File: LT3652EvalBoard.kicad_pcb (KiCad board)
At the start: 2 copper layers, 55.2 x 50.3 mm, 42 parts, among them U1 LT3652

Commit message: Fixed project info
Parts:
- Dbat1, Dflybk1, Dvin1: footprint diodes:DIODES_INC_ZLLS500 -> ms_diodes:DIODES_INC_ZLLS500
- Lsw1: footprint inductors:PANASONIC_ELC09D100F -> ms_inductors:PANASONIC_ELC09D100F
- Pload2: footprint connectors:WURTH_ELEKTRONIK_629104151021 -> ms_connectors:WURTH_ELEKTRONIK_629104151021
- RV1, RV2: footprint bourns_trim_pots:Bourns_3362P_Trimmer -> ms_bourns_trim_pots:Bourns_3362P_Trimmer
- Wbat1, Wgnd1, Wshdn1, Wsw1, Wvfb1, Wvreg1: footprint pcb_test_points:HARWIN_S1751-46 -> ms_pcb_test_points:HARWIN_S1751-46
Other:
- board text added: "LT3652 Eval Board Rev 0.3 15-03-2016"
- board text added: "https://github.com/malcolmspiteri/LT3652EvalBoard"
- board text removed: "LT3652 Eval Board Rev 0.3"
- board text removed: "Url: https://github.com/malcolmspiteri/LT3652EvalBoard Date: 13-03-2016"

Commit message: Rev 0.3 Final - onto Rev 0.4 now to make the board smaller hence cheaper to manufacture
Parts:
- U1: footprint ms_lt3652:LT3652MSE_HandSoldering -> ms_lt3652:LT3652MSE
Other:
- rule pad_to_mask_clearance: 0.2 -> 0.055
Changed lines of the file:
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@@
     (pad_size 1.524 1.524)
     (pad_drill 0.762)
-    (pad_to_mask_clearance 0.2)
+    (pad_to_mask_clearance 0.055)
     (aux_axis_origin 147.866 107.95)
     (grid_origin 147.066 107.95)
@@
     )
   )
-  (module ms_lt3652:LT3652MSE_HandSoldering (layer F.Cu)
-    (at 138.666 98.75)
-    (fp_text reference U1 (at 0.02 3.49) (layer F.SilkS)
-      (effects (font (size 0.5 0.5) (thickness 0.075)))
-    )
-    (fp_text value LT3652 (at 0 2.64) (layer F.Fab)
-      (effects (font (size 0.5 0.5) (thickness 0.075)))
-    )
-    (pad 6 smd rect (at -2.258 1.6075 90) (size 0.42 1.3) (layers F.Cu F.Paste F.Mask)
-      (net 6 "Net-(JP1-Pad2)") (solder_mask_margin 0.05))
-    (pad 5 smd rect (at -2.258 0.9575 90) (size 0.42 1.3) (layers F.Cu F.Paste F.Mask)
-      (net 10 "Net-(R2-Pad1)") (solder_mask_margin 0.05))
-    (pad 4 smd rect (at -2.258 0.3075 90) (size 0.42 1.3) (layers F.Cu F.Paste F.Mask)
-      (net 9 "Net-(R1-Pad1)") (solder_mask_margin 0.05))
-    (pad 3 smd rect (at -2.258 -0.3425 90) (size 0.42 1.3) (layers F.Cu F.Paste F.Mask)
-      (net 5 /SHDN) (solder_mask_margin 0.05))
-    (pad 2 smd rect (at -2.258 -0.9925 90) (size 0.42 1.3) (layers F.Cu F.Paste F.Mask)
-      (net 4 /VIN_REG) (solder_mask_margin 0.05))
-    (pad 1 smd rect (at -2.258 -1.6425 90) (size 0.42 1.3) (layers F.Cu F.Paste F.Mask)
-      (net 3 /VIN) (solder_mask_margin 0.05))
-    (pad 12 smd rect (at 2.253 -1.6425 90) (size 0.42 1.3) (layers F.Cu F.Paste F.Mask)
-      (net 17 /SW) (solder_mask_margin 0.05))
-    (pad 11 smd rect (at 2.253 -0.9925 90) (size 0.42 1.3) (layers F.Cu F.Paste F.Mask)
-      (net 16 /BOOST) (solder_mask_margin 0.05))
-    (pad 10 smd rect (at 2.253 -0.3425 90) (size 0.42 1.3) (layers F.Cu F.Paste F.Mask)
-      (net 19 /SENSE) (solder_mask_margin 0.05))
-    (pad 9 smd rect (at 2.253 0.3075 90) (size 0.42 1.3) (layers F.Cu F.Paste F.Mask)
-      (net 15 /BAT) (solder_mask_margin 0.05))
-    (pad 8 smd rect (at 2.253 0.9575 90) (size 0.42 1.3) (layers F.Cu F.Paste F.Mask)
-      (solder_mask_margin 0.05))
-    (pad 7 smd rect (at 2.253 1.6075 90) (size 0.42 1.3) (layers F.Cu F.Paste F.Mask)
-      (net 18 /VFB) (solder_mask_margin 0.05))
-    (pad 13 smd rect (at -0.0075 -0.0175 90) (size 2.845 1.7) (layers F.Cu F.Paste F.Mask)
-      (net 2 GND))
-  )
   (module ms_diodes:DIODES_INC_ZLLS500 (layer F.Cu)
     (at 149.066 104.25)
@@
   (module ms_connectors:WURTH_ELEKTRONIK_629104151021 (layer F.Cu)
     (at 162.466 87.75 90)
-    (fp_text reference Pload2 (at 0 9.6 90) (layer F.SilkS)
+    (fp_text reference Pload2 (at 8.6 -2 180) (layer F.SilkS)
       (effects (font (size 1 1) (thickness 0.15)))
     )
@@
       (net 4 /VIN_REG))
   )
+  (module ms_lt3652:LT3652MSE (layer F.Cu)
+    (at 138.666 98.75)
+    (fp_text reference U1 (at 0.02 3.49) (layer F.SilkS)
+      (effects (font (size 0.5 0.5) (thickness 0.075)))
+    )
+    (fp_text value LT3652 (at 0 2.64) (layer F.Fab)
+      (effects (font (size 0.5 0.5) (thickness 0.075)))
+    )
+    (pad 6 smd rect (at -2.1025 1.6075 90) (size 0.42 0.989) (layers F.Cu F.Paste F.Mask)
+      (net 6 "Net-(JP1-Pad2)"))
+    (pad 5 smd rect (at -2.1025 0.9575 90) (size 0.42 0.989) (layers F.Cu F.Paste F.Mask)
+      (net 10 "Net-(R2-Pad1)"))
+    (pad 4 smd rect (at -2.1025 0.3075 90) (size 0.42 0.989) (layers F.Cu F.Paste F.Mask)
+      (net 9 "Net-(R1-Pad1)"))
+    (pad 3 smd rect (at -2.1025 -0.3425 90) (size 0.42 0.989) (layers F.Cu F.Paste F.Mask)
+      (net 5 /SHDN))
+    (pad 2 smd rect (at -2.1025 -0.9925 90) (size 0.42 0.989) (layers F.Cu F.Paste F.Mask)
+      (net 4 /VIN_REG))
+    (pad 1 smd rect (at -2.1025 -1.6425 90) (size 0.42 0.989) (layers F.Cu F.Paste F.Mask)
+      (net 3 /VIN))
+    (pad 12 smd rect (at 2.0975 -1.6425 90) (size 0.42 0.989) (layers F.Cu F.Paste F.Mask)
+      (net 17 /SW))
+    (pad 11 smd rect (at 2.0975 -0.9925 90) (size 0.42 0.989) (layers F.Cu F.Paste F.Mask)
+      (net 16 /BOOST))
+    (pad 10 smd rect (at 2.0975 -0.3425 90) (size 0.42 0.989) (layers F.Cu F.Paste F.Mask)
+      (net 19 /SENSE))
+    (pad 9 smd rect (at 2.0975 0.3075 90) (size 0.42 0.989) (layers F.Cu F.Paste F.Mask)
+      (net 15 /BAT))
+    (pad 8 smd rect (at 2.0975 0.9575 90) (size 0.42 0.989) (layers F.Cu F.Paste F.Mask))
+    (pad 7 smd rect (at 2.0975 1.6075 90) (size 0.42 0.989) (layers F.Cu F.Paste F.Mask)
+      (net 18 /VFB))
+    (pad 13 smd rect (at -0.0075 -0.0175 90) (size 2.845 1.7) (layers F.Cu F.Paste F.Mask)
+      (net 2 GND))
+  )
   (gr_line (start 162.666 120.55) (end 161.366 120.55) (angle 90) (layer F.SilkS) (width 0.2))

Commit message: Upload of Rev 0.5
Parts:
- removed the ? at (143.9, 95.8)
- removed Pload2: USB_A, ms_connectors:WURTH_ELEKTRONIK_629104151021
- added REF**: MHH-20_ABS_Plastic_Box, ms_enclosures:MHH-20_ABS_Plastic_Box_Holes_Only, F.Cu at (135.4, 89.7)
- added Wvin1: TEST_1P, ms_pcb_test_points:HARWIN_S1751-46, F.Cu at (119.6, 68.4)
- Pbat1, Pload1: footprint w_conn_jst-ph:b2b-ph-kl -> w_conn_jst-ph:s2b-ph-kl
- U1: footprint ms_lt3652:LT3652MSE -> ms_lt3652:LT3652MSE_HandSoldering
- moved Pload1 28.8 mm to (153.3, 76.2)
- moved Cbat1 27.3 mm to (147.3, 75.7), turned to 180 degrees
- moved Wbat1 23.2 mm to (152.3, 85.7), turned to 90 degrees
- moved JPload1 18.1 mm to (152.6, 91.7), turned to 0 degrees
- moved Pbat1 16.0 mm to (153.3, 102.7)
- moved ? 9.92 mm to (136.4, 109.7)
- moved C3 8.42 mm to (140.3, 94.5)
- moved R1 8.42 mm to (125.8, 92.8)
- moved R2 8.42 mm to (125.8, 95.3)
- moved Cbs1 8.42 mm to (137.7, 89.8)
- moved Dvin1 8.42 mm to (127.0, 74.2)
- moved JP3 8.42 mm to (120.0, 91.5)
- moved Lsw1 8.42 mm to (136.7, 78.8)
- moved Pled1 8.42 mm to (125.4, 107.8)
- moved Pslr1 8.42 mm to (127.0, 69.0)
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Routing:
- net Net-(Dvin1-Pad3): track 44.9 -> 48.3 mm
- net /VIN: track 88.6 -> 91.6 mm
- net /BAT: track 56.7 -> 57.8 mm
- net Net-(Cbat1-Pad1): track 28.0 -> 27.1 mm
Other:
- board size 55.2 x 50.3 mm -> 49.8 x 49.8 mm
- board text added: "LT3652 Eval Board Rev 0.5 21-03-2016"
- board text removed: "LT3652 Eval Board Rev 0.3 15-03-2016"

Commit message: Rev 0.6 - Adds ability to add solar panel in series, plus separate blocking diode for parallel solar panel
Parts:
- added Dvin2: ZLLS500, ms_diodes:DIODES_INC_ZLLS500, F.Cu at (131.1, 74.2)
- added JPnl1: JUMPER3, Pin_Headers:Pin_Header_Straight_1x03, F.Cu at (149.3, 74.2)
- added Pslr3: JST PH, w_conn_jst-ph:b2b-ph-kl, F.Cu at (132.8, 69.0)
- Dvin1: value D_Schottky_Small_ZLLS500 -> ZLLS500
- moved Cbat1 8.78 mm to (155.6, 78.7), turned to 90 degrees
- moved Pload1 8.75 mm to (153.1, 85.0)
- moved Wbat1 8.16 mm to (157.6, 92.0), turned to 270 degrees
- moved Pslr2 3.85 mm to (141.3, 69.0)
- moved Pslr1 2.65 mm to (124.3, 69.0)
- moved Wvin1 2.61 mm to (117.1, 68.0)
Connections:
- Pslr1 pad 2: GND -> Net-(JPnl1-Pad2)
- Pslr2 pad 1: Net-(Dvin1-Pad3) -> Net-(Dvin2-Pad3)
- RV1 pad 1: Net-(Dvin1-Pad3) -> /VIN
- RV2 pad 1: Net-(Dvin1-Pad3) -> /VIN
- Wvin1 pad 1: Net-(Dvin1-Pad3) -> /VIN
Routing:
- net Net-(Dvin1-Pad3): track 48.3 -> 5.64 mm
- net /VIN: track 91.6 -> 127.9 mm
- net Net-(JPnl1-Pad2): track 0.00 -> 28.4 mm
- net Net-(JPnl1-Pad3): track 0.00 -> 13.3 mm
- net Net-(Dvin2-Pad3): track 0.00 -> 12.1 mm
- net Net-(Cbat1-Pad1): track 27.1 -> 19.3 mm
- net /BAT: track 57.8 -> 56.8 mm
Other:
- board text added: "(PAR)"
- board text added: "GND"
- board text added: "LT3652 Eval Board Rev 0.6 24-03-2016"
- board text added: "SER"
- board text removed: "LT3652 Eval Board Rev 0.5 21-03-2016"

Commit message: Minor alignment fix
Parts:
- moved Pload1 0.25 mm to (153.3, 85.0)
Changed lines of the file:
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@@
     (links 70)
     (no_connects 0)
-    (area 109.990999 65.274999 159.941001 115.225001)
+    (area 109.676715 62.92484 162.63554 117.28582)
     (thickness 1.6)
     (drawings 22)
@@
   )
   (setup
-    (last_trace_width 0.5)
+    (last_trace_width 0.25)
     (user_trace_width 0.3)
     (user_trace_width 0.4)
@@
   )
   (module w_conn_jst-ph:s2b-ph-kl (layer F.Cu)
-    (at 153.066 84.95 90)
+    (at 153.316 84.95 90)
     (descr "JST PH series connector, S2B-PH-KL")
     (fp_text reference Pload1 (at 0 -2.79908 90) (layer F.SilkS)

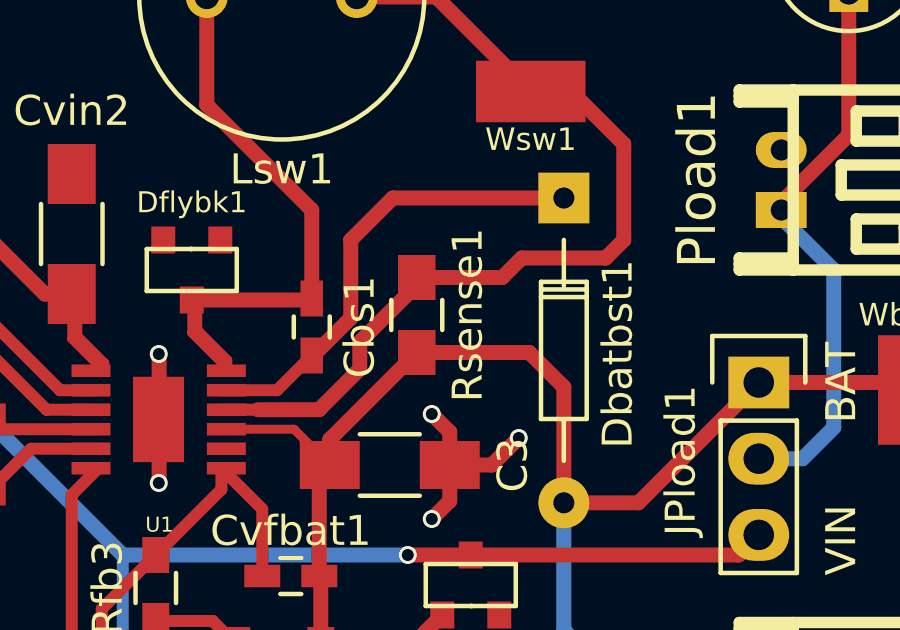
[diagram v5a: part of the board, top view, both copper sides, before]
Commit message: Fixed wrong footprint for Rsense1
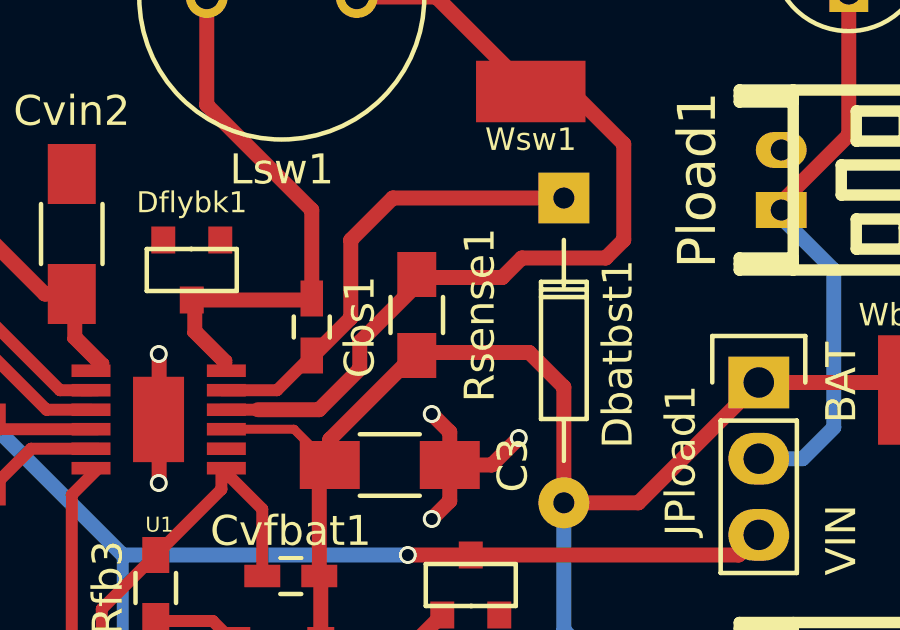
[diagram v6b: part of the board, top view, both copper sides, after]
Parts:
- Rsense1: footprint Capacitors_SMD:C_0805_HandSoldering -> Resistors_SMD:R_0805_HandSoldering
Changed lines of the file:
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@@
-    )
-  )
-  (module Capacitors_SMD:C_0805_HandSoldering (layer F.Cu)
-    (at 141.166 89.45 270)
-    (descr "Capacitor SMD 0805, hand soldering")
-    (tags "capacitor 0805")
-    (attr smd)
-    (fp_text reference Rsense1 (at 0 -1.7 270) (layer F.SilkS)
-      (effects (font (size 1 1) (thickness 0.15)))
-    )
-    (fp_text value 250mO (at 0 2.1 270) (layer F.Fab)
-      (effects (font (size 1 1) (thickness 0.15)))
-    )
-    (fp_line (start -2.3 -1) (end 2.3 -1) (layer F.CrtYd) (width 0.05))
-    (fp_line (start -2.3 1) (end 2.3 1) (layer F.CrtYd) (width 0.05))
-    (fp_line (start -2.3 -1) (end -2.3 1) (layer F.CrtYd) (width 0.05))
-    (fp_line (start 2.3 -1) (end 2.3 1) (layer F.CrtYd) (width 0.05))
-    (fp_line (start 0.5 -0.85) (end -0.5 -0.85) (layer F.SilkS) (width 0.15))
-    (fp_line (start -0.5 0.85) (end 0.5 0.85) (layer F.SilkS) (width 0.15))
-    (pad 1 smd rect (at -1.25 0 270) (size 1.5 1.25) (layers F.Cu F.Paste F.Mask)
-      (net 19 /SENSE))
-    (pad 2 smd rect (at 1.25 0 270) (size 1.5 1.25) (layers F.Cu F.Paste F.Mask)
-      (net 15 /BAT))
-    (model Capacitors_SMD.3dshapes/C_0805_HandSoldering.wrl
-      (at (xyz 0 0 0))
-      (scale (xyz 1 1 1))
-      (rotate (xyz 0 0 0))
     )
   )
@@
       (at (xyz 0 0 0))
       (scale (xyz 1 1 1))
+      (rotate (xyz 0 0 0))
+    )
+  )
+  (module Resistors_SMD:R_0805_HandSoldering (layer F.Cu)
+    (at 141.166 89.45 270)
+    (descr "Resistor SMD 0805, hand soldering")
+    (tags "resistor 0805")
+    (attr smd)
+    (fp_text reference Rsense1 (at 0 -2.1 270) (layer F.SilkS)
+      (effects (font (size 1 1) (thickness 0.15)))
+    )
+    (fp_text value 250mO (at 0 2.1 270) (layer F.Fab)
+      (effects (font (size 1 1) (thickness 0.15)))
+    )
+    (fp_line (start -2.4 -1) (end 2.4 -1) (layer F.CrtYd) (width 0.05))
+    (fp_line (start -2.4 1) (end 2.4 1) (layer F.CrtYd) (width 0.05))
+    (fp_line (start -2.4 -1) (end -2.4 1) (layer F.CrtYd) (width 0.05))
+    (fp_line (start 2.4 -1) (end 2.4 1) (layer F.CrtYd) (width 0.05))
+    (fp_line (start 0.6 0.875) (end -0.6 0.875) (layer F.SilkS) (width 0.15))
+    (fp_line (start -0.6 -0.875) (end 0.6 -0.875) (layer F.SilkS) (width 0.15))
+    (pad 1 smd rect (at -1.35 0 270) (size 1.5 1.3) (layers F.Cu F.Paste F.Mask)
+      (net 19 /SENSE))
+    (pad 2 smd rect (at 1.35 0 270) (size 1.5 1.3) (layers F.Cu F.Paste F.Mask)
+      (net 15 /BAT))
+    (model Resistors_SMD.3dshapes/R_0805_HandSoldering.wrl
+      (at (xyz 0 0 0))
+      (scale (xyz 1 1 1))

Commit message: Rev 0.7
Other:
- board text added: "LT3652 Eval Board Rev 0.7 29-03-2016"
- board text removed: "LT3652 Eval Board Rev 0.6 24-03-2016"
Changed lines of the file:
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@@
   (title_block
     (title "LT3652 Evaluation Board")
-    (date 2016-03-24)
-    (rev 0.6)
+    (date 2016-03-29)
+    (rev 0.7)
     (company "Malcolm Spiteri")
   )
@@
       (net 17 /SW))
   )
-  (module ms_bourns_trim_pots:Bourns_3362P_Trimmer (layer F.Cu)
-    (at 114.266 77.65 180)
-    (fp_text reference RV1 (at -4.3 2.3 270) (layer F.SilkS)
-      (effects (font (size 1 1) (thickness 0.15)))
-    )
-    (fp_text value POT (at 0 2.51 180) (layer F.Fab)
-      (effects (font (size 1 1) (thickness 0.15)))
-    )
-    (fp_line (start 3.3 3.54) (end -3.3 3.54) (layer F.SilkS) (width 0.15))
-    (fp_line (start -3.3 3.54) (end -3.3 -3.46) (layer F.SilkS) (width 0.15))
-    (fp_line (start -3.3 -3.46) (end 3.3 -3.46) (layer F.SilkS) (width 0.15))
-    (fp_line (start 3.3 -3.46) (end 3.3 3.54) (layer F.SilkS) (width 0.15))
-    (pad 2 thru_hole circle (at 0 -2.53) (size 1.397 1.397) (drill 0.8128) (layers *.Cu *.Mask F.SilkS)
-      (net 4 /VIN_REG))
-    (pad 3 thru_hole circle (at -2.54 0.01) (size 1.397 1.397) (drill 0.8128) (layers *.Cu *.Mask F.SilkS)
-      (net 24 "Net-(RV1-Pad3)"))
-    (pad 1 thru_hole circle (at 2.54 0.01) (size 1.397 1.397) (drill 0.8128) (layers *.Cu *.Mask F.SilkS)
-      (net 3 /VIN))
-  )
-  (module ms_bourns_trim_pots:Bourns_3362P_Trimmer (layer F.Cu)
-    (at 114.266 85.45 180)
-    (fp_text reference RV2 (at -4.3 2.3 270) (layer F.SilkS)
-      (effects (font (size 1 1) (thickness 0.15)))
-    )
-    (fp_text value POT (at 0 2.51 180) (layer F.Fab)
-      (effects (font (size 1 1) (thickness 0.15)))
-    )
-    (fp_line (start 3.3 3.54) (end -3.3 3.54) (layer F.SilkS) (width 0.15))
-    (fp_line (start -3.3 3.54) (end -3.3 -3.46) (layer F.SilkS) (width 0.15))
-    (fp_line (start -3.3 -3.46) (end 3.3 -3.46) (layer F.SilkS) (width 0.15))
-    (fp_line (start 3.3 -3.46) (end 3.3 3.54) (layer F.SilkS) (width 0.15))
-    (pad 2 thru_hole circle (at 0 -2.53) (size 1.397 1.397) (drill 0.8128) (layers *.Cu *.Mask F.SilkS)
-      (net 5 /SHDN))
-    (pad 3 thru_hole circle (at -2.54 0.01) (size 1.397 1.397) (drill 0.8128) (layers *.Cu *.Mask F.SilkS)
-      (net 23 "Net-(RV2-Pad3)"))
-    (pad 1 thru_hole circle (at 2.54 0.01) (size 1.397 1.397) (drill 0.8128) (layers *.Cu *.Mask F.SilkS)
-      (net 3 /VIN))
-  )
   (module ms_pcb_test_points:HARWIN_S1751-46 (layer F.Cu)
     (at 117.066 67.95)
@@
     )
   )
+  (module ms_bourns_trim_pots:Bourns_3362P_Trimmer (layer F.Cu)
+    (at 114.266 77.65 180)
+    (fp_text reference RV1 (at -4.3 2.2 270) (layer F.SilkS)
+      (effects (font (size 1 1) (thickness 0.15)))
+    )
+    (fp_text value POT (at 0 2.51 180) (layer F.Fab)
+      (effects (font (size 1 1) (thickness 0.15)))
+    )
+    (fp_line (start 3.3 3.54) (end -3.3 3.54) (layer F.SilkS) (width 0.15))
+    (fp_line (start -3.3 3.54) (end -3.3 -3.46) (layer F.SilkS) (width 0.15))
+    (fp_line (start -3.3 -3.46) (end 3.3 -3.46) (layer F.SilkS) (width 0.15))
+    (fp_line (start 3.3 -3.46) (end 3.3 3.54) (layer F.SilkS) (width 0.15))
+    (pad 2 thru_hole circle (at 0 -2.53) (size 1 1) (drill 0.5) (layers *.Cu *.Mask F.SilkS)
+      (net 4 /VIN_REG))
+    (pad 3 thru_hole circle (at -2.54 0.01) (size 1 1) (drill 0.5) (layers *.Cu *.Mask F.SilkS)
+      (net 24 "Net-(RV1-Pad3)"))
+    (pad 1 thru_hole circle (at 2.54 0.01) (size 1 1) (drill 0.5) (layers *.Cu *.Mask F.SilkS)
+      (net 3 /VIN))
+  )
+  (module ms_bourns_trim_pots:Bourns_3362P_Trimmer (layer F.Cu)
+    (at 114.266 85.45 180)
+    (fp_text reference RV2 (at -4.3 2.25 270) (layer F.SilkS)
+      (effects (font (size 1 1) (thickness 0.15)))
+    )
+    (fp_text value POT (at 0 2.51 180) (layer F.Fab)
+      (effects (font (size 1 1) (thickness 0.15)))
+    )
+    (fp_line (start 3.3 3.54) (end -3.3 3.54) (layer F.SilkS) (width 0.15))
+    (fp_line (start -3.3 3.54) (end -3.3 -3.46) (layer F.SilkS) (width 0.15))
+    (fp_line (start -3.3 -3.46) (end 3.3 -3.46) (layer F.SilkS) (width 0.15))
+    (fp_line (start 3.3 -3.46) (end 3.3 3.54) (layer F.SilkS) (width 0.15))
+    (pad 2 thru_hole circle (at 0 -2.53) (size 1 1) (drill 0.5) (layers *.Cu *.Mask F.SilkS)
+      (net 5 /SHDN))
+    (pad 3 thru_hole circle (at -2.54 0.01) (size 1 1) (drill 0.5) (layers *.Cu *.Mask F.SilkS)
+      (net 23 "Net-(RV2-Pad3)"))
+    (pad 1 thru_hole circle (at 2.54 0.01) (size 1 1) (drill 0.5) (layers *.Cu *.Mask F.SilkS)
+      (net 3 /VIN))
+  )
   (gr_text "(PAR)" (at 147.066 68.95 90) (layer F.SilkS)
     (effects (font (size 1 1) (thickness 0.15)))
@@
     (effects (font (size 1 1) (thickness 0.15)))
   )
-  (gr_text "LT3652 \nEval Board\nRev 0.6\n24-03-2016" (at 140.966 110.45) (layer F.SilkS)
+  (gr_text "LT3652 \nEval Board\nRev 0.7\n29-03-2016" (at 140.966 110.45) (layer F.SilkS)
     (effects (font (size 1.1 1.2) (thickness 0.2)) (justify left))
   )

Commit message: Rev 0.9
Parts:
- added Wsw0: TEST_1P, ms_pcb_test_points:HARWIN_S1751-46, F.Cu at (129.1, 78.8)
- moved Pslr2 17.0 mm to (124.4, 69.0)
- moved Wbat1 16.2 mm to (146.0, 103.2), turned to 0 degrees
- moved Pslr1 8.35 mm to (132.7, 69.0)
- moved Pslr3 8.25 mm to (141.1, 69.0)
- moved Dvin2 5.40 mm to (125.7, 74.2)
- moved Dvin1 3.70 mm to (130.7, 74.2)
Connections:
- Pbat1 pad 1: /BAT -> GND
- Pbat1 pad 2: GND -> /BAT
- Pload1 pad 1: Net-(Cbat1-Pad1) -> GND
- Pload1 pad 2: GND -> Net-(Cbat1-Pad1)
- Pslr1 pad 1: Net-(Dvin1-Pad3) -> Net-(JPnl1-Pad2)
- Pslr1 pad 2: Net-(JPnl1-Pad2) -> Net-(Dvin1-Pad3)
- Pslr2 pad 1: Net-(Dvin2-Pad3) -> GND
- Pslr2 pad 2: GND -> Net-(Dvin2-Pad3)
- Pslr3 pad 1: Net-(JPnl1-Pad3) -> GND
- Pslr3 pad 2: GND -> Net-(JPnl1-Pad3)
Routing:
- net /VIN: track 127.9 -> 116.4 mm
- net Net-(JPnl1-Pad2): track 28.4 -> 17.7 mm
- net Net-(Dvin2-Pad3): track 12.1 -> 6.25 mm
- net Net-(JPnl1-Pad3): track 13.3 -> 7.87 mm
- net /SW: track 21.3 -> 26.4 mm
- net /BAT: track 56.8 -> 53.2 mm
- net Net-(Dvin1-Pad3): track 5.64 -> 4.22 mm
- net GND: track 11.0 -> 12.4 mm, vias 5 -> 6
- net Net-(Cbat1-Pad1): track 19.3 -> 20.1 mm
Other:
- board text added: "LT3652 Eval Board Rev 0.9 10-04-2016"
- board text removed: "(PAR)"
- board text removed: "LT3652 Eval Board Rev 0.7 29-03-2016"
